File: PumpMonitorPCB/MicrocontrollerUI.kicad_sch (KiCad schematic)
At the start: 23 parts, among them J2 Debug, SW1 EN, SW2 BOOT, SW3 OK, SW4 OK, SW5 OK, U3 MC14504B, U4 ESP32-S3-WROOM-1

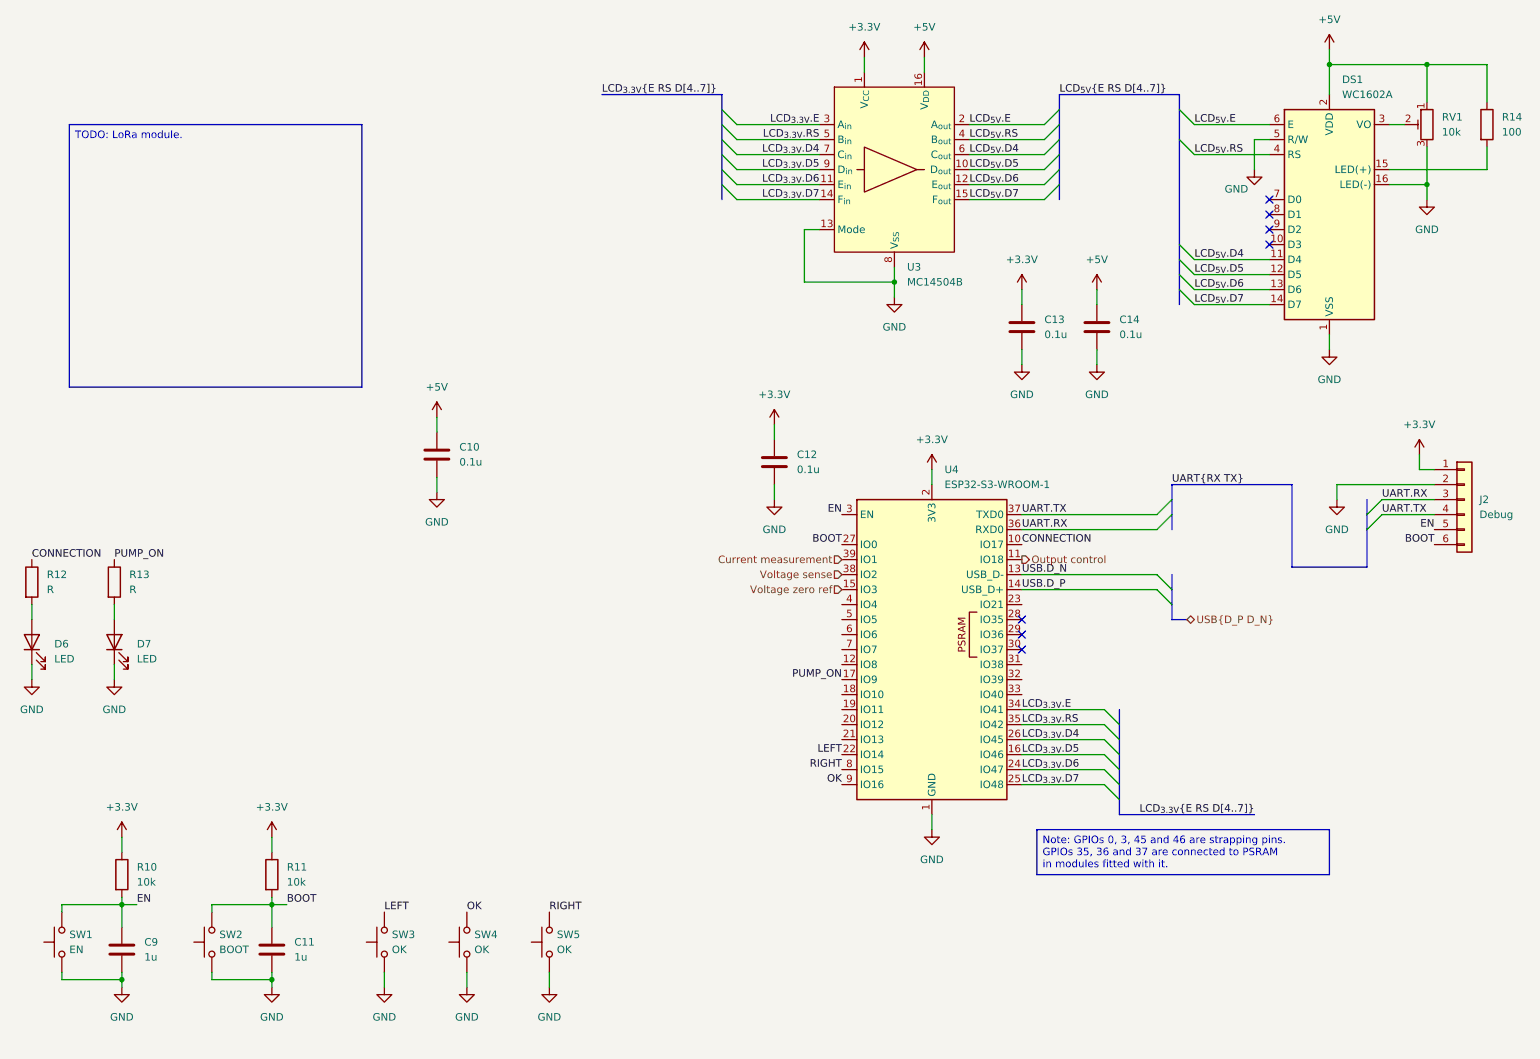
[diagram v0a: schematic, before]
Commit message: Tidied schematic, added LoRa module.
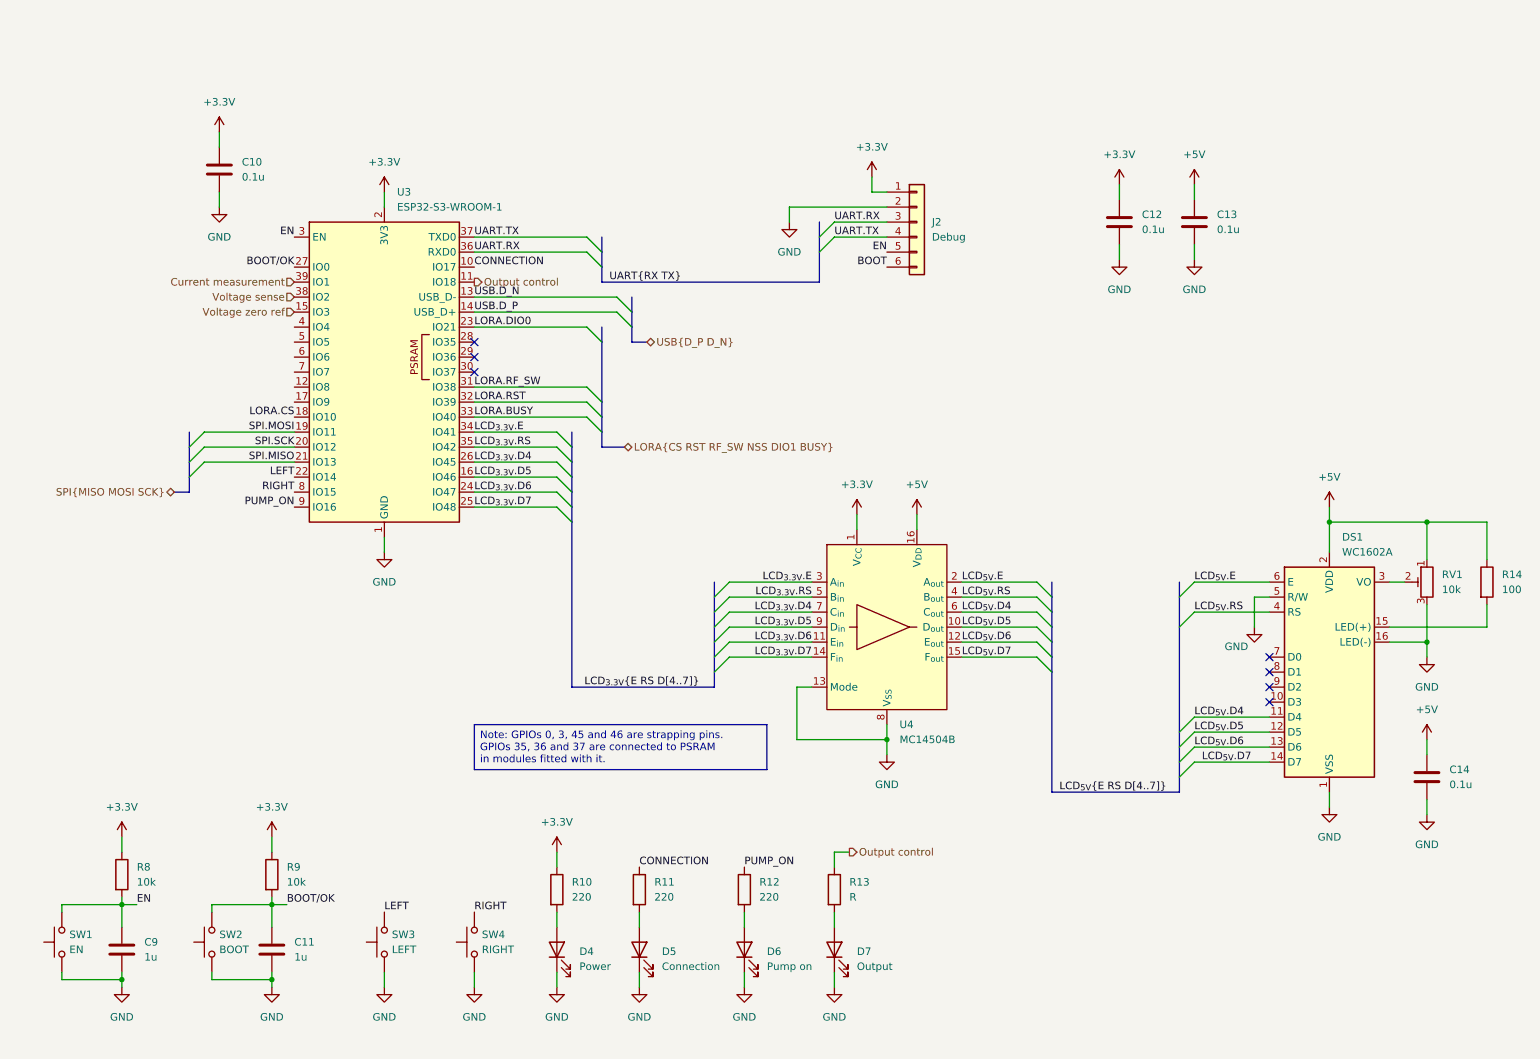
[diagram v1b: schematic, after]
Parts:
- removed SW4: OK, Button_Switch_SMD:SW_Push_1P1T_NO_CK_KMR2, symbol Switch:SW_Push
- added D4: Power, symbol Device:LED
- added D7: Output, symbol Device:LED
- added R10: 220, symbol Device:R
- added R13: R, symbol Device:R
- D5: renamed from D6; value LED -> Connection
- D6: renamed from D7; value LED -> Pump on
- R11: renamed from R12; value R -> 220
- R12: renamed from R13; value R -> 220
- SW3: value OK -> LEFT
- SW4: renamed from SW5; value OK -> RIGHT
- renumbered C12 to C10, C13 to C12, C14 to C13, C10 to C14, R10 to R8, R11 to R9, U4 to U3, U3 to U4
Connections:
- net OK is gone; now on net PUMP_ON: U3.9 (IO16)
- net +3.3V: now also R10.1
- net BOOT: no longer C11.2, R9.2, SW2.2, U3.27 (IO0)
- net GND: now also D4.1 (K), D7.1 (K)
- net Output control: now also R13.1
- net PUMP_ON: no longer U3.17 (IO9)
- net LORA.CS: now reaches U3.18 (IO10)
- net SPI.MOSI: now reaches U3.19 (IO11)
- net SPI.SCK: now reaches U3.20 (IO12)
- net SPI.MISO: now reaches U3.21 (IO13)
- net LORA.DIO0: now reaches U3.23 (IO21)
- net LORA.RF_SW: now reaches U3.31 (IO38)
- net LORA.RST: now reaches U3.32 (IO39)
- net LORA.BUSY: now reaches U3.33 (IO40)
- new net: D7.2 (A), R13.2
- new net: D4.2 (A), R10.2
- new net BOOT/OK: C11.2, R9.2, SW2.2, U3.27 (IO0)
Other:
- moved on the sheet: C10, C12, C13, C14, D5, D6, DS1, J2, R11, R12, R14, RV1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

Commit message: Added aux. connectors, started assigning components.
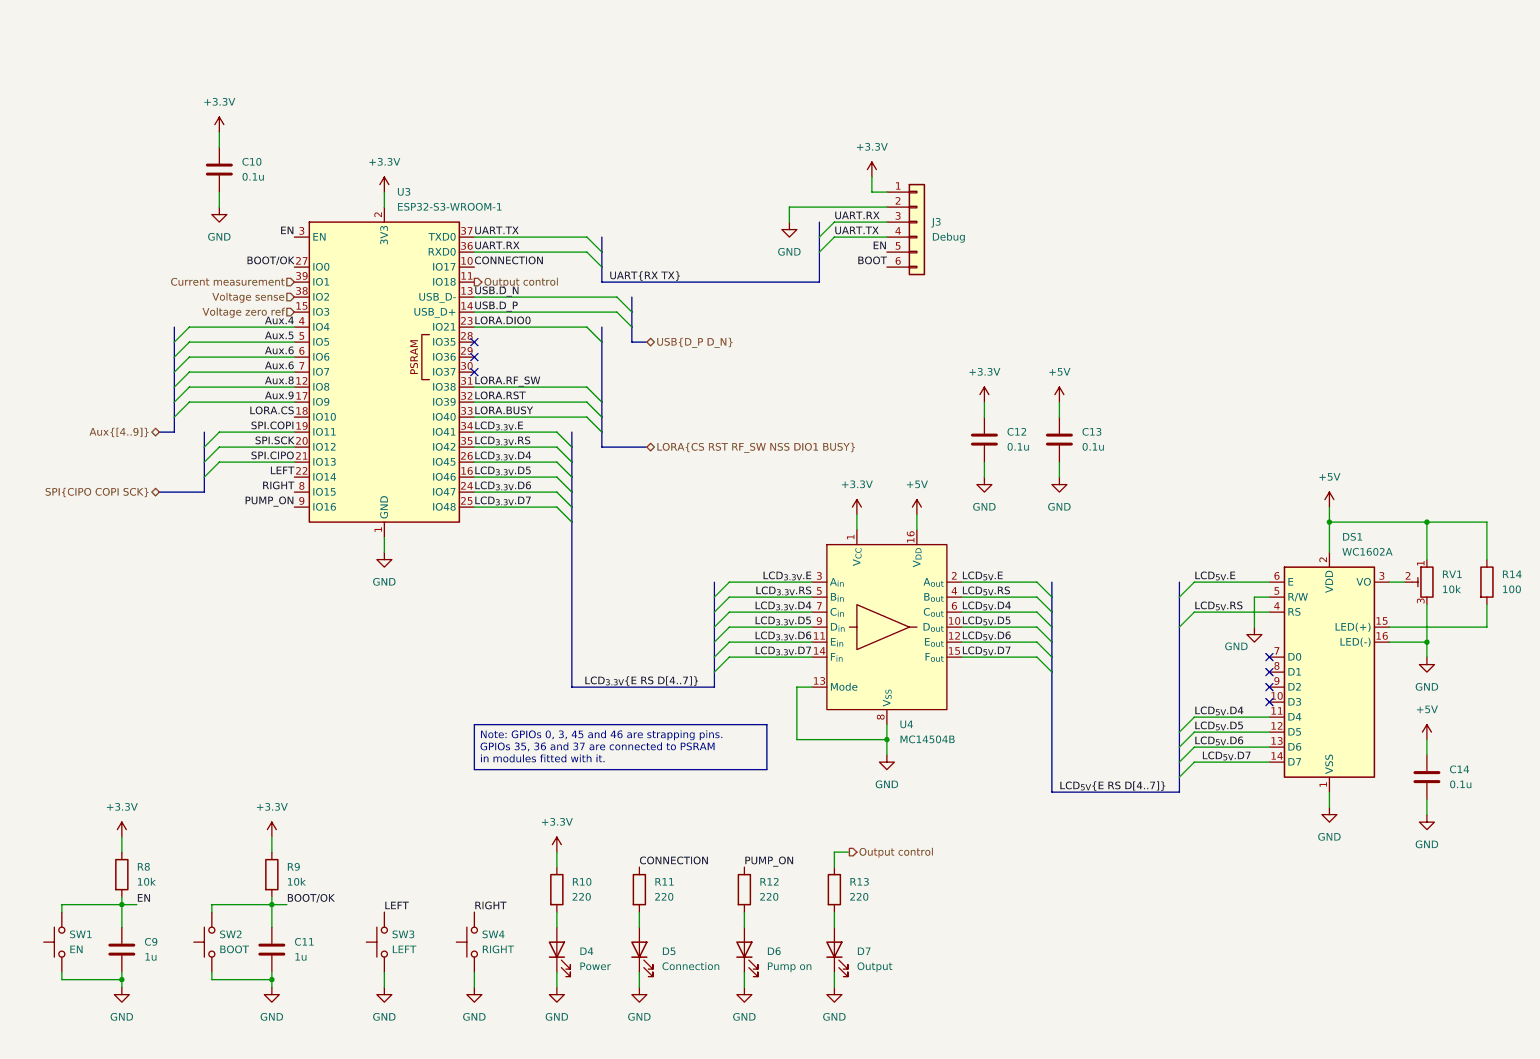
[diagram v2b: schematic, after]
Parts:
- C10, C12, C13, C14: footprint (none) -> Capacitor_SMD:C_0805_2012Metric_Pad1.18x1.45mm_HandSolder
- C11, C9: footprint Capacitor_SMD:C_0603_1608Metric_Pad1.08x0.95mm_HandSolder -> Capacitor_SMD:C_0805_2012Metric_Pad1.18x1.45mm_HandSolder
- D4, D5, D6, D7: footprint (none) -> LED_THT:LED_D5.0mm
- J3: renamed from J2; footprint (none) -> Connector_PinHeader_2.54mm:PinHeader_1x06_P2.54mm_Vertical
- R10, R11, R12: footprint (none) -> Resistor_SMD:R_0805_2012Metric_Pad1.20x1.40mm_HandSolder
- R13: value R -> 220; footprint (none) -> Resistor_SMD:R_0805_2012Metric_Pad1.20x1.40mm_HandSolder
- R14: footprint (none) -> Resistor_THT:R_Axial_DIN0207_L6.3mm_D2.5mm_P7.62mm_Horizontal
- SW1, SW2, SW3, SW4: footprint Button_Switch_SMD:SW_Push_1P1T_NO_CK_KMR2 -> (none)
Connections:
- net Aux.8: now reaches U3.12 (IO8)
- net Aux.9: now reaches U3.17 (IO9)
- net Aux.4: now reaches U3.4 (IO4)
- net Aux.5: now reaches U3.5 (IO5)
- net Aux.6: now reaches U3.6 (IO6)
- net Aux.6: now also U3.7 (IO7)
- net SPI.MISO renamed SPI.CIPO
- net SPI.MOSI renamed SPI.COPI
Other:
- moved on the sheet: C12, C13

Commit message: Added op amps to voltage and current measurement, more footprint assignments.
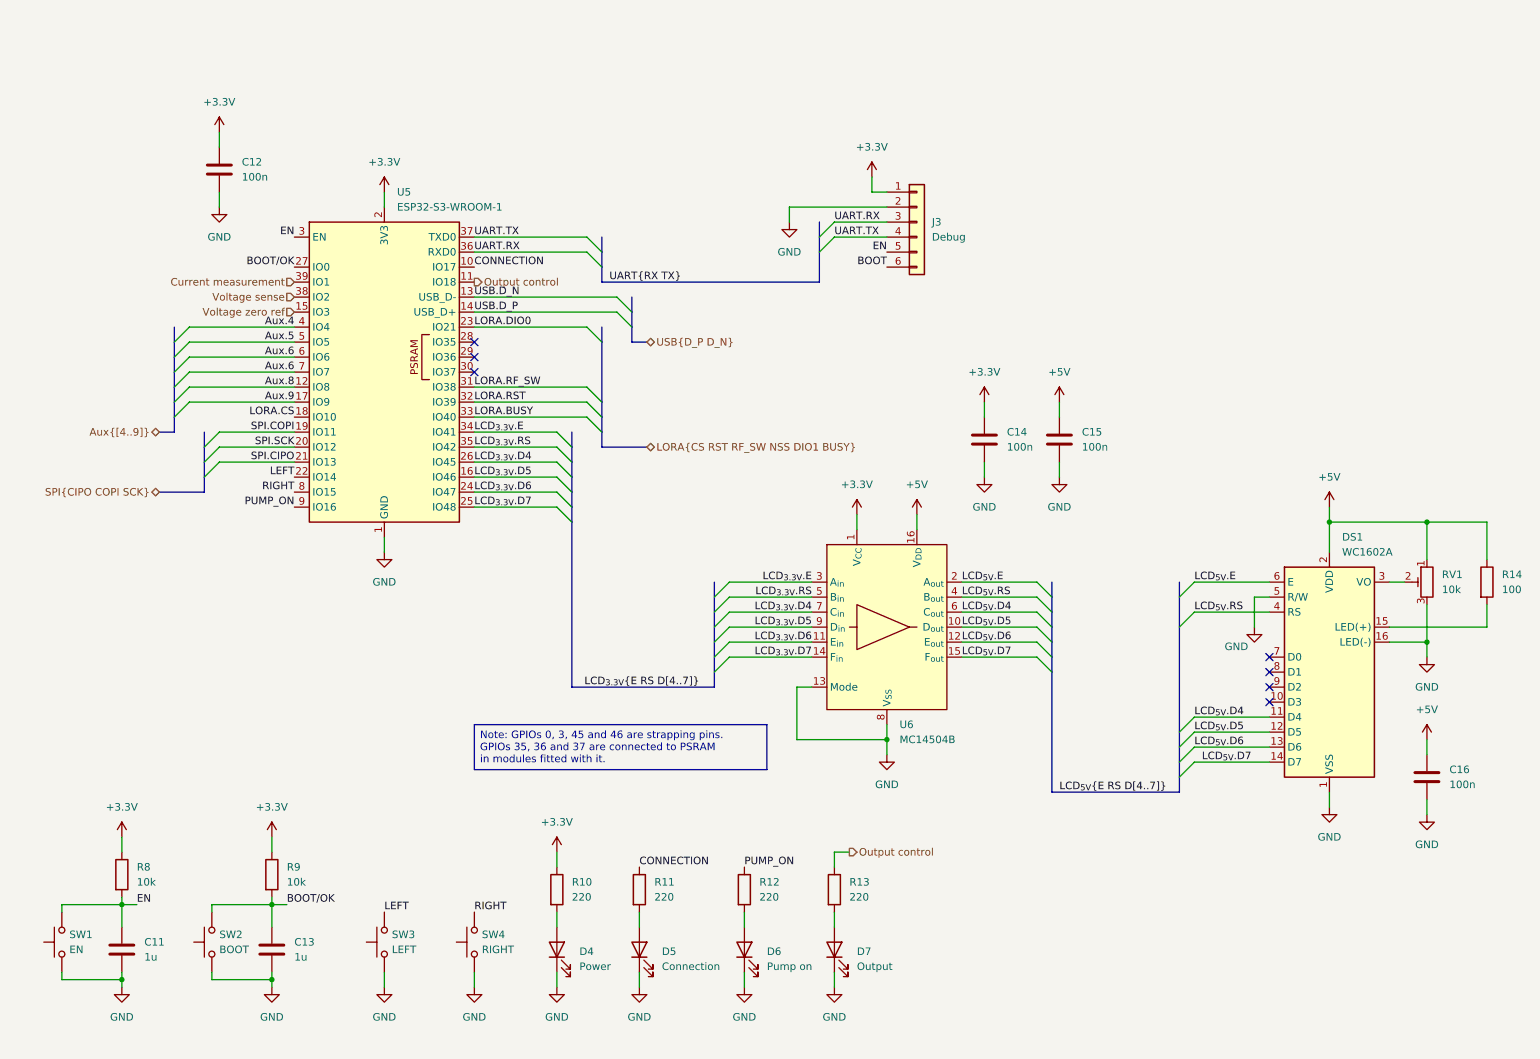
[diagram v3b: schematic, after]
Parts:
- C12: renamed from C10; value 0.1u -> 100n
- C14: renamed from C12; value 0.1u -> 100n
- C15: renamed from C13; value 0.1u -> 100n
- C16: renamed from C14; value 0.1u -> 100n
- renumbered C9 to C11, C11 to C13, U3 to U5, U4 to U6

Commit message: Added terminals footprint and 3D model.
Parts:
- RV1: footprint (none) -> Potentiometer_THT:Potentiometer_ACP_CA9-V10_Vertical
- SW1: footprint (none) -> Button_Switch_THT:SW_Tactile_SPST_Angled_PTS645Vx39-2LFS
- SW2, SW3, SW4: footprint (none) -> Connector_PinHeader_2.54mm:PinHeader_1x02_P2.54mm_Vertical
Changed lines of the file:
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@@
 			)
 		)
-		(property "Footprint" ""
+		(property "Footprint" "Connector_PinHeader_2.54mm:PinHeader_1x02_P2.54mm_Vertical"
 			(at 90.17 172.72 0)
 			(effects
@@
 			)
 		)
-		(property "Footprint" ""
+		(property "Footprint" "Potentiometer_THT:Potentiometer_ACP_CA9-V10_Vertical"
 			(at 256.54 111.76 0)
 			(effects
@@
 		(pin "2"
 		)
+		(instances
+			(project "PumpMonitorPCB"
+				(path "/c90c4964-ca1b-44d9-8ea9-8989903af0f2/519408a1-89cc-4bd2-9b7b-cb03d2ff4d33/d8d6cf40-f9ad-44cc-b7dc-bac9eac23749"
+					(reference "RV1")
+					(unit 1)
+				)
+			)
+		)
 	)
 	(symbol
@@
 		(pin "22"
 		)
+		(instances
+			(project "PumpMonitorPCB"
+				(path "/c90c4964-ca1b-44d9-8ea9-8989903af0f2/519408a1-89cc-4bd2-9b7b-cb03d2ff4d33/d8d6cf40-f9ad-44cc-b7dc-bac9eac23749"
+					(reference "U5")
+					(unit 1)
+				)
+			)
+		)
 	)
 	(symbol
@@
 		(pin "5"
 		)
+		(instances
+			(project "PumpMonitorPCB"
+				(path "/c90c4964-ca1b-44d9-8ea9-8989903af0f2/519408a1-89cc-4bd2-9b7b-cb03d2ff4d33/d8d6cf40-f9ad-44cc-b7dc-bac9eac23749"
+					(reference "J3")
+					(unit 1)
+				)
+			)
+		)
 	)
 	(symbol
@@
 		(pin "2"
 		)
+		(instances
+			(project "PumpMonitorPCB"
+				(path "/c90c4964-ca1b-44d9-8ea9-8989903af0f2/519408a1-89cc-4bd2-9b7b-cb03d2ff4d33/d8d6cf40-f9ad-44cc-b7dc-bac9eac23749"
+					(reference "R14")
+					(unit 1)
+				)
+			)
+		)
 	)
 	(symbol
@@
 		(pin "1"
 		)
+		(instances
+			(project "PumpMonitorPCB"
+				(path "/c90c4964-ca1b-44d9-8ea9-8989903af0f2/519408a1-89cc-4bd2-9b7b-cb03d2ff4d33/d8d6cf40-f9ad-44cc-b7dc-bac9eac23749"
+					(reference "R12")
+					(unit 1)
+				)
+			)
+		)
 	)
 	(symbol
@@
 		(pin "2"
 		)
+		(instances
+			(project "PumpMonitorPCB"
+				(path "/c90c4964-ca1b-44d9-8ea9-8989903af0f2/519408a1-89cc-4bd2-9b7b-cb03d2ff4d33/d8d6cf40-f9ad-44cc-b7dc-bac9eac23749"
+					(reference "R11")
+					(unit 1)
+				)
+			)
+		)
 	)
 	(symbol
@@
 			)
 		)
-		(property "Footprint" ""
+		(property "Footprint" "Connector_PinHeader_2.54mm:PinHeader_1x02_P2.54mm_Vertical"
 			(at 45.72 172.72 0)
 			(effects
@@
 		(pin "3"
 		)
+		(instances
+			(project "PumpMonitorPCB"
+				(path "/c90c4964-ca1b-44d9-8ea9-8989903af0f2/519408a1-89cc-4bd2-9b7b-cb03d2ff4d33/d8d6cf40-f9ad-44cc-b7dc-bac9eac23749"
+					(reference "U6")
+					(unit 1)
+				)
+			)
+		)
 	)
 	(symbol
@@
 		(pin "2"
 		)
+		(instances
+			(project "PumpMonitorPCB"
+				(path "/c90c4964-ca1b-44d9-8ea9-8989903af0f2/519408a1-89cc-4bd2-9b7b-cb03d2ff4d33/d8d6cf40-f9ad-44cc-b7dc-bac9eac23749"
+					(reference "D5")
+					(unit 1)
+				)
+			)
+		)
 	)
 	(symbol
@@
 		(pin "1"
 		)
+		(instances
+			(project "PumpMonitorPCB"
+				(path "/c90c4964-ca1b-44d9-8ea9-8989903af0f2/519408a1-89cc-4bd2-9b7b-cb03d2ff4d33/d8d6cf40-f9ad-44cc-b7dc-bac9eac23749"
+					(reference "D6")
+					(unit 1)
+				)
+			)
+		)
 	)
 	(symbol
@@
 		(pin "1"
 		)
+		(instances
+			(project "PumpMonitorPCB"
+				(path "/c90c4964-ca1b-44d9-8ea9-8989903af0f2/519408a1-89cc-4bd2-9b7b-cb03d2ff4d33/d8d6cf40-f9ad-44cc-b7dc-bac9eac23749"
+					(reference "DS1")
+					(unit 1)
+				)
+			)
+		)
 	)
 	(symbol
@@
 			)
 		)
-		(property "Footprint" ""
+		(property "Footprint" "Button_Switch_THT:SW_Tactile_SPST_Angled_PTS645Vx39-2LFS"
 			(at 20.32 172.72 0)
 			(effects
@@
 			)
 		)
-		(property "Footprint" ""
+		(property "Footprint" "Connector_PinHeader_2.54mm:PinHeader_1x02_P2.54mm_Vertical"
 			(at 74.93 172.72 0)
 			(effects
